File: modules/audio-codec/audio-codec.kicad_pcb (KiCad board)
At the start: 2 copper layers, 20.3 x 28.3 mm, 24 parts, among them U1 TLV320AIC3110IRHBR, U2 ADP5301ACBZ-1-R7

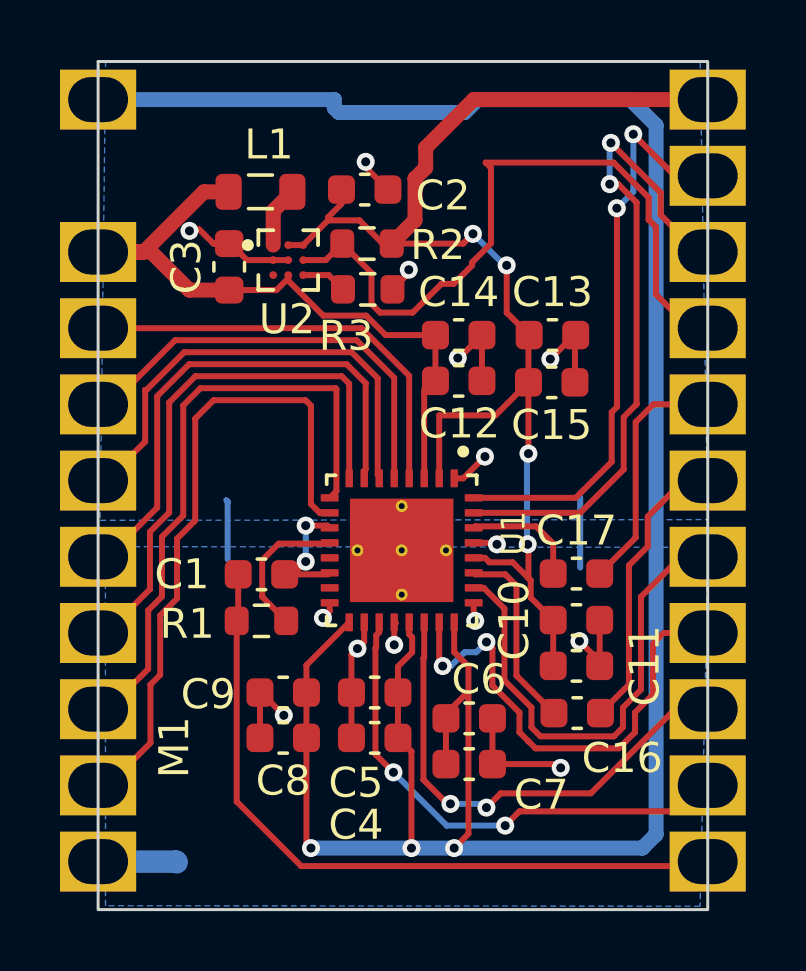
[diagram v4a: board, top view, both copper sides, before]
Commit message: outstanding changes to audio codec module
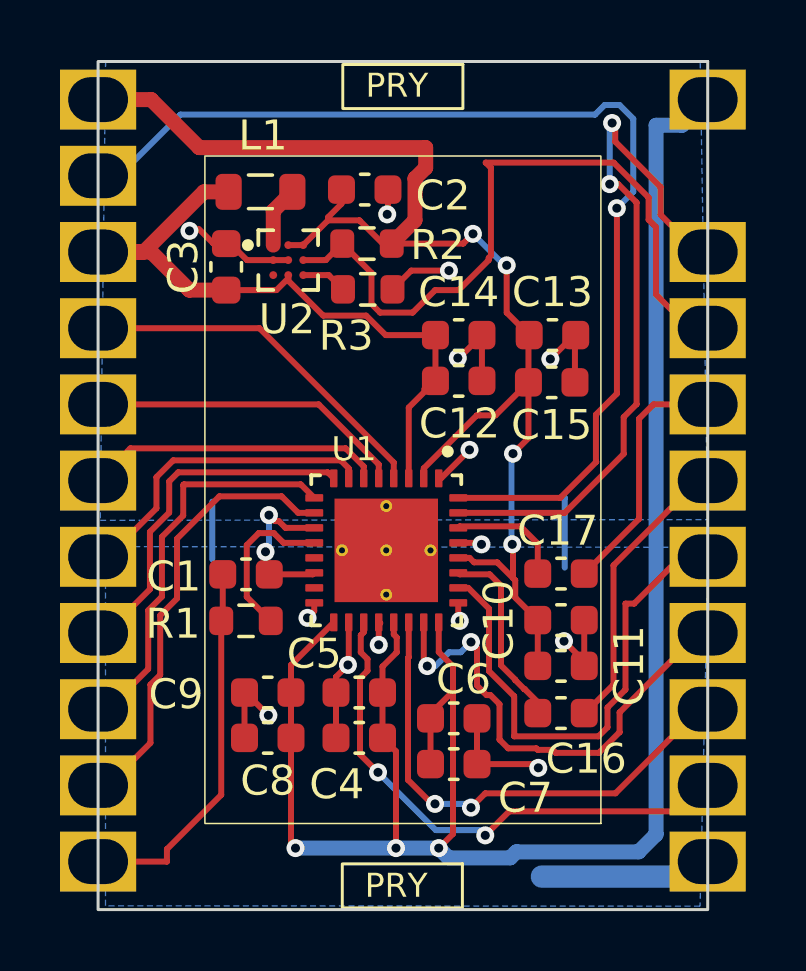
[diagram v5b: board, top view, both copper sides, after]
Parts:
- M1: moved to B.Cu
- moved C16 0.54 mm to (89.9, 70.8)
- moved C1 0.52 mm to (79.4, 66.2)
- moved C10 0.52 mm to (89.9, 67.7)
- moved C11 0.52 mm to (89.9, 69.2)
- moved C17 0.52 mm to (89.9, 66.2)
- moved C4 0.52 mm to (83.2, 71.6)
- moved C5 0.52 mm to (83.2, 70.1)
- moved C6 0.52 mm to (86.4, 71.0)
- moved C7 0.52 mm to (86.4, 72.5)
- moved C8 0.52 mm to (80.2, 71.6)
- moved C9 0.52 mm to (80.2, 70.1)
- moved R1 0.52 mm to (79.4, 67.7)
- moved U1 0.52 mm to (84.1, 65.4)
- moved C3 0.10 mm to (78.8, 55.9)
- turned M1 to 180 degrees
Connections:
- M1 pad 10: SCL -> SPEAKER_L_M
- M1 pad 14: /RESET -> DECOUPLE5
- M1 pad 15: V1.8_MODE -> I2S_DOUT
- M1 pad 16: 3.5MM_RIGHT -> I2S_DIN
- M1 pad 17: 3.5MM_LEFT -> WCLK
- M1 pad 18: SPEAKER_R_P -> I2S_BCLK
- M1 pad 19: SPEAKER_R_M -> I2S_MCLK
- M1 pad 20: SPEAKER_L_P -> SDA
- M1 pad 21: SPEAKER_L_M -> SCL
- M1 pad 3: DECOUPLE5 -> /RESET
- M1 pad 4: I2S_DOUT -> V1.8_MODE
- M1 pad 5: I2S_DIN -> 3.5MM_RIGHT
- M1 pad 6: WCLK -> 3.5MM_LEFT
- M1 pad 7: I2S_BCLK -> SPEAKER_R_P
- M1 pad 8: I2S_MCLK -> SPEAKER_R_M
- M1 pad 9: SDA -> SPEAKER_L_P
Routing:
- net GPIO1: track 19.4 -> 36.1 mm, vias 2 -> 1
- net DECOUPLE1: track 81.6 -> 65.7 mm
- net 3.5MM_MIC: track 24.2 -> 12.6 mm
- net SDA: track 20.6 -> 13.4 mm
- net SCL: track 22.0 -> 14.9 mm
- net I2S_MCLK: track 18.4 -> 11.9 mm
- net I2S_BCLK: track 17.2 -> 11.0 mm
- net WCLK: track 15.8 -> 10.2 mm
- net GND: track 35.2 -> 40.3 mm
- net I2S_DIN: track 14.6 -> 11.1 mm
- net I2S_DOUT: track 14.4 -> 12.2 mm
- net /RESET: track 23.4 -> 24.9 mm
- net SPEAKER_L_M: track 17.1 -> 18.0 mm
- net Net-(U1-MIC1RP): track 4.43 -> 5.28 mm
- net 3.5MM_LEFT: track 9.70 -> 10.4 mm
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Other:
- board text added: "Audio Codec R20250212"
- board text added: "megaphone-r5-modular"

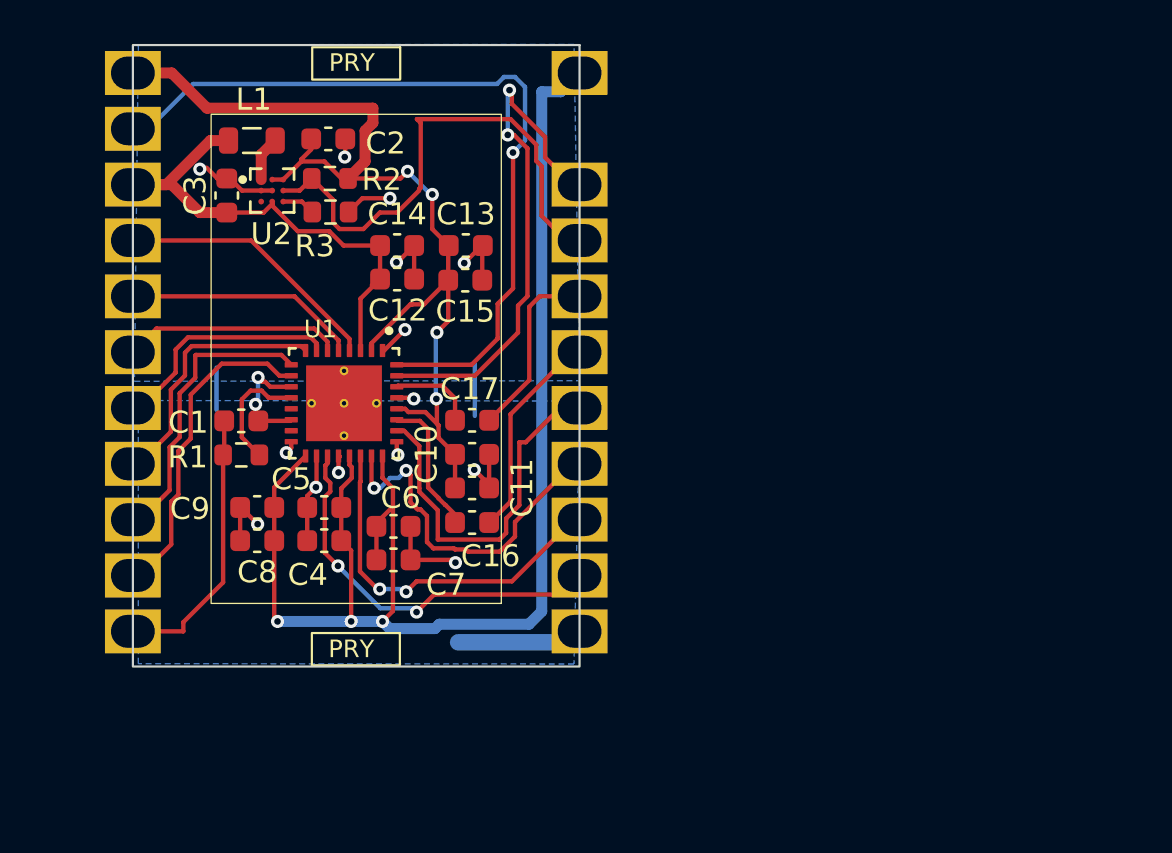
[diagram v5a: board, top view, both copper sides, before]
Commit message: update audio codec module footprint and generate gerbers
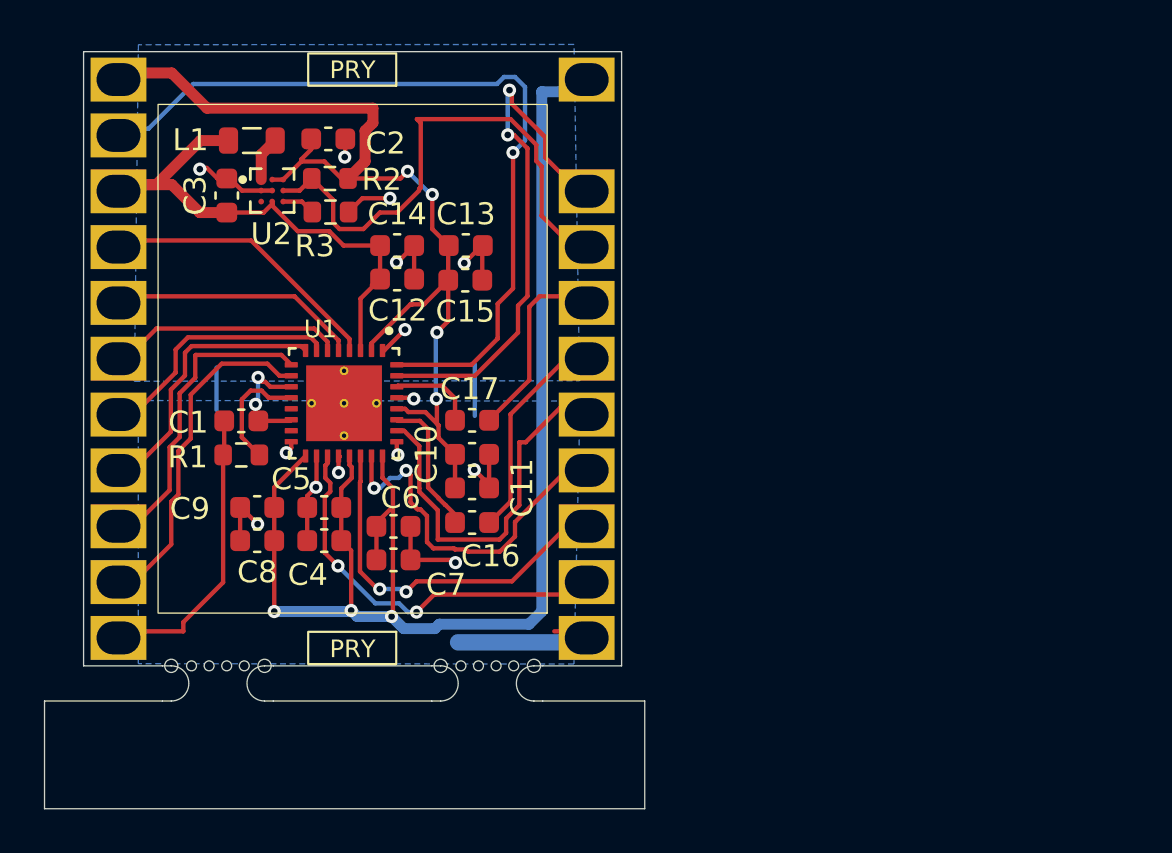
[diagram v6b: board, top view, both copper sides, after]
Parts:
- M1: footprint MegaCastle:MegaCastle2x11Wide-Module-I13.2x22.25 -> MegaCastle:MegaCastle2x11-Module-I17.7x23.1-MBFFFFC-PANEL-NIBBLE
- moved M1 1.58 mm to (84.5, 63.4)
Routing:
- net DECOUPLE1: track 65.7 -> 64.7 mm
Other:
- board size 20.3 x 28.3 mm -> 24.5 x 29.5 mm
- board text added: "Audio Codec R20250219"
- board text removed: "Audio Codec R20250212"

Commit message: Updating audio-codec
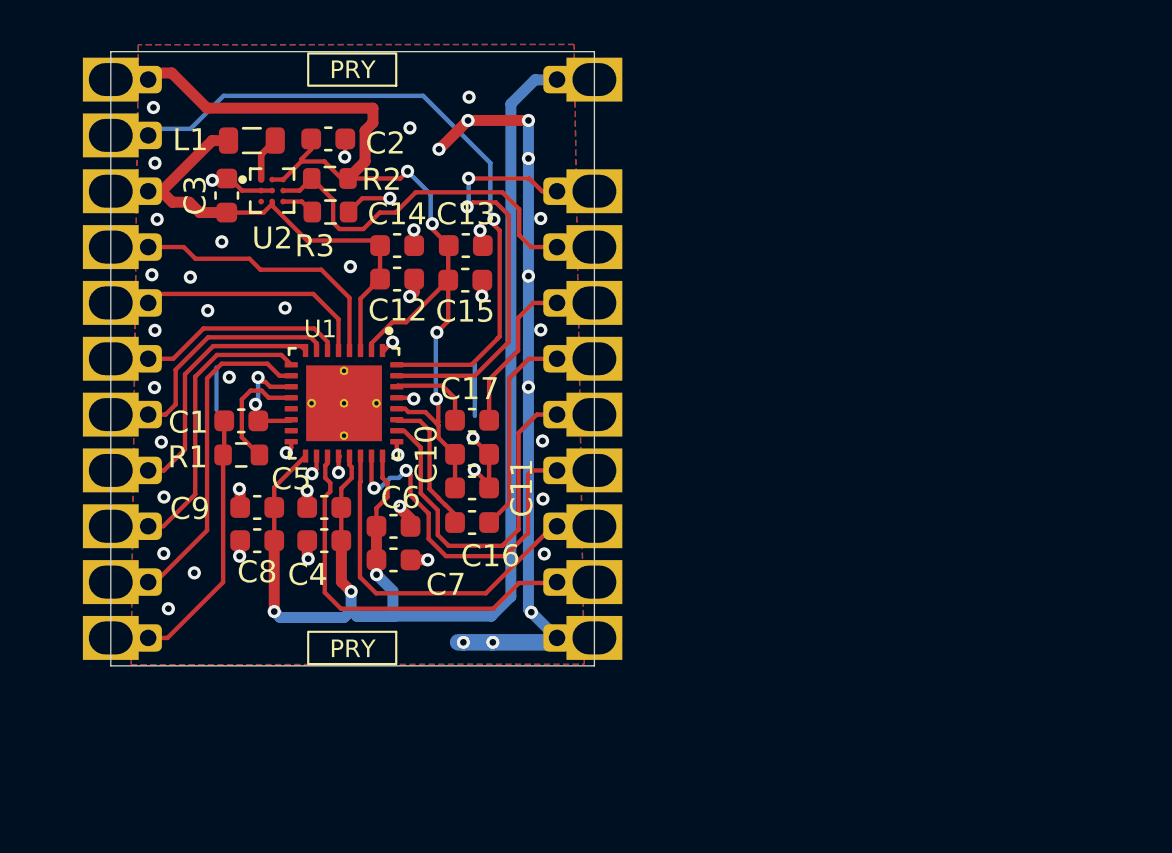
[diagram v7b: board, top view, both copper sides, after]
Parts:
- M1: footprint MegaCastle:MegaCastle2x11-Module-I17.7x23.1-MBFFFFC-PANEL-NIBBLE -> MegaCastle:MegaCastle2x11-Module-I22.0x23.1-MBFFFFC-SPAREPAD
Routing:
- net GND: track 40.3 -> 62.0 mm, vias 14 -> 54
- net V1.8_MODE: track 22.9 -> 16.7 mm
- net /RESET: track 24.9 -> 19.3 mm
- net GPIO1: track 36.1 -> 31.4 mm
- net DECOUPLE1: track 64.7 -> 63.2 mm
- net DECOUPLE5: track 23.8 -> 22.4 mm
- net 3.5MM_RIGHT: track 8.40 -> 7.26 mm
- net 3.5MM_LEFT: track 10.4 -> 9.47 mm
- net SPEAKER_L_P: track 17.0 -> 16.1 mm, vias 2 -> 0
- net 3.5MM_MIC: track 12.6 -> 11.8 mm
- net SPEAKER_R_P: track 16.9 -> 16.4 mm
- net SPEAKER_L_M: track 18.0 -> 17.8 mm, vias 2 -> 0
- added copper zone on F.Cu, net GND
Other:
- board size 24.5 x 29.5 mm -> 22 x 27.9 mm
